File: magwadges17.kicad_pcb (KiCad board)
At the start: 2 copper layers, 156 x 89.8 mm, 52 parts, among them J1 PGM, J2 JACK_2P, U1 ATTINY861A-SU

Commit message: Start to add LCSC parts
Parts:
- C1: footprint SM0805 -> Capacitor_SMD:C_0805_2012Metric
- D1, D2, D3, D4: footprint SM0805 -> LED_SMD:LED_0805_2012Metric
- J1: footprint Pin_Headers:Pin_Header_Straight_2x03_Pitch2.54mm_SMD -> Connector_PinHeader_2.54mm:PinHeader_2x03_P2.54mm_Vertical_SMD
- RN1: footprint NETWORK1206 -> Resistor_SMD:R_Array_Concave_4x0603
- RN2: value RLED -> 10k; footprint NETWORK1206 -> Resistor_SMD:R_Array_Concave_4x0603
- S1, S2, S3, S4, S5, S6, S7, S8: footprint custom:PTS645 -> Button_Switch_SMD:SW_SPST_PTS645
- U1: footprint Housings_SOIC:SOIC-20W_7.5x12.8mm_Pitch1.27mm -> Package_SO:SOIC-20W_7.5x12.8mm_P1.27mm
- turned RN1 to -20 degrees
- turned RN2 to -45 degrees
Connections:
- S1 pad 2: (no net) -> unconnected-(S1-Pad2)
- S2 pad 2: (no net) -> unconnected-(S2-Pad2)
- S3 pad 2: (no net) -> unconnected-(S3-Pad2)
- S4 pad 2: (no net) -> unconnected-(S4-Pad2)
- S5 pad 2: (no net) -> unconnected-(S5-Pad2)
- S6 pad 2: (no net) -> unconnected-(S6-Pad2)
- S7 pad 2: (no net) -> unconnected-(S7-Pad2)
- S8 pad 2: (no net) -> unconnected-(S8-Pad2)
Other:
- net class Default removed

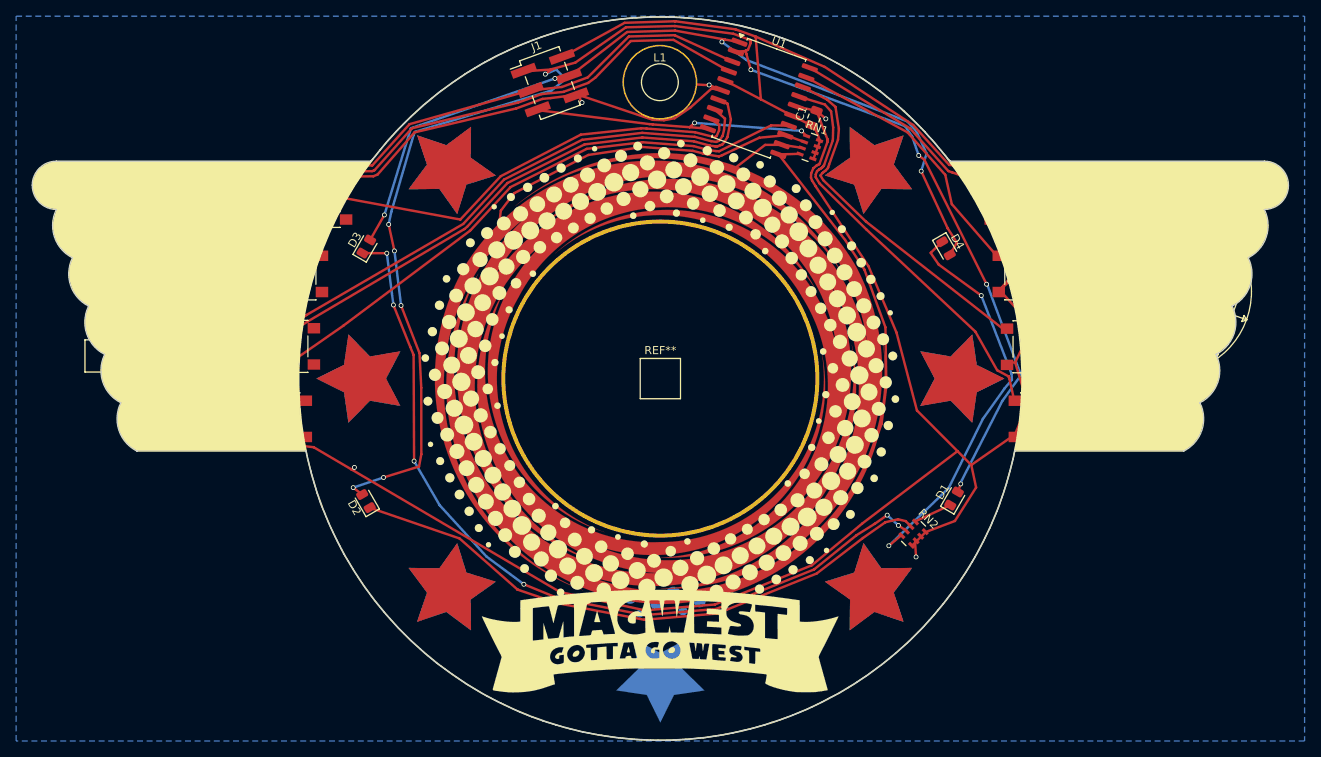
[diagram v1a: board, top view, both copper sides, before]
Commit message: Clean up board, rip traces
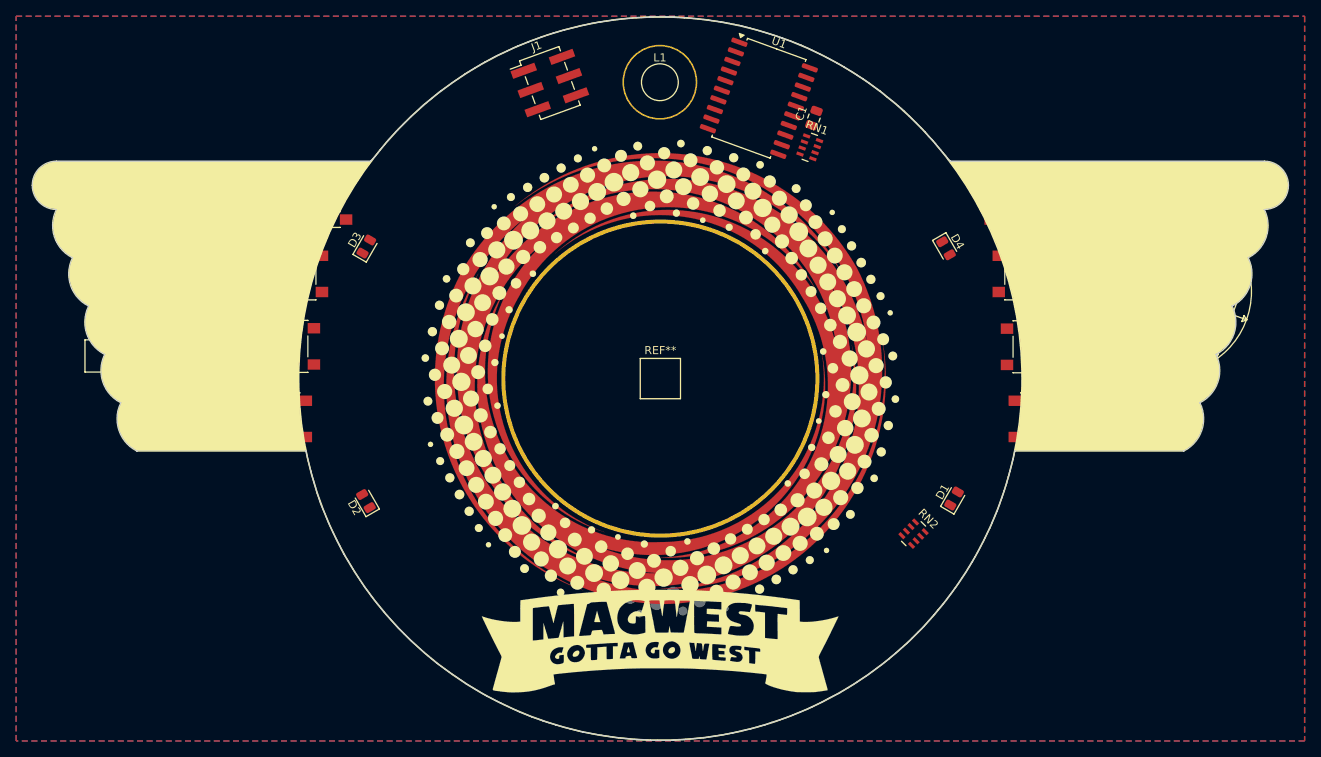
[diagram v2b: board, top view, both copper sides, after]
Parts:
- removed G14, G15, G16, G18 (x2), G19, G20, G21, G22, G23, G25, G26, G27: LOGO, custom:test_star4_copper
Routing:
- net GND: track 411.1 -> 0.00 mm, vias 9 -> 0
- net Net-(D1-A): track 183.4 -> 0.00 mm, vias 10 -> 0
- net VCC: track 141.5 -> 0.00 mm, vias 2 -> 0
- net Net-(U1-(ADC7/~{OC1D}/CLKI/XTAL1/PCINT12)PB4): track 110.2 -> 0.00 mm
- net Net-(U1-(ADC8/OC1D/CLKO/XTAL2/PCINT13)PB5): track 106.4 -> 0.00 mm
- net Net-(D3-A): track 102.9 -> 0.00 mm, vias 4 -> 0
- net Net-(D3-K): track 102.1 -> 0.00 mm, vias 6 -> 0
- net SW_F: track 85.1 -> 0.00 mm
- net SW_E: track 79.6 -> 0.00 mm
- net SW_G: track 74.4 -> 0.00 mm
- net Net-(D2-K): track 74.1 -> 0.00 mm
- net SW_H: track 60.7 -> 0.00 mm
- net SW_D: track 51.6 -> 0.00 mm
- net Net-(D4-K): track 49.5 -> 0.00 mm, vias 2 -> 0
- net TouchC: track 45.0 -> 0.00 mm
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- added copper zone on F.Cu, net GND
